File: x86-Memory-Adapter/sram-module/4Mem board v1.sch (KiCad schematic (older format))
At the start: 35 parts, among them K1 CONN_3, P1 CONN_1, P11 CONN_2X2, P2 CONN_1, P3 CONN_1, P4 CONN_1, P8 CONN_20X2, P9 CONN_20X2, U1 SRAM_128KB, U14 XC9536XL-VQ44, U2 SRAM_128KB, U3 SRAM_128KB, U4 SRAM_128KB, U7 LM1086CS_TO252_DPAK

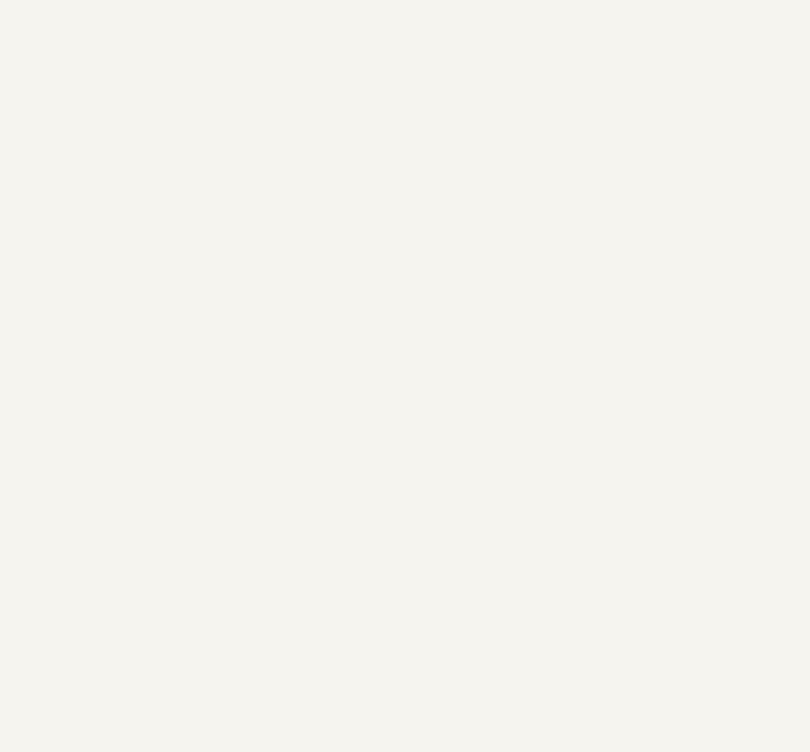
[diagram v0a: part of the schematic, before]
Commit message: x86-Memory-Adapter: SRAM module spare SRAM_512KB symbol (off-sheet)
Source: S100 4GB DRAM BOARD/4Mem board v1 (working folder)
The SRAM_512KB symbol is unannotated, placed outside the sheet and is not in the netlist.
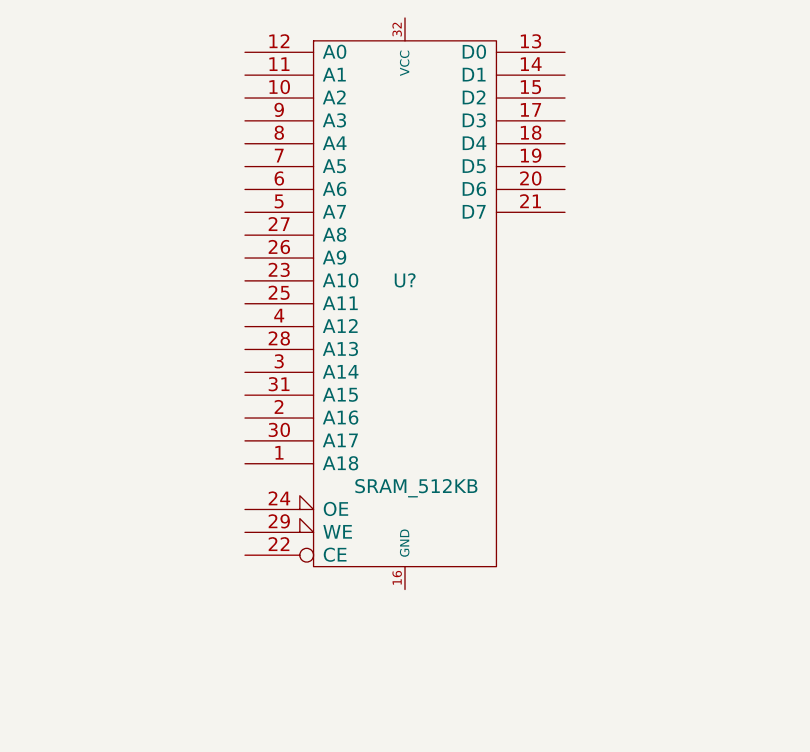
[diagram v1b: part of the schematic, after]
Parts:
- added U?: SRAM_512KB, ~, symbol SRAM_512KB
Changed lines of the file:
@@
 LIBS:numato_kicad_lib
 LIBS:ANTS_MOD1
+LIBS:xc6slx45-2fgg484c
 LIBS:4Mem board v1-cache
 EELAYER 27 0
@@
 Sheet 1 1
 Title "noname.sch"
-Date "29 apr 2015"
+Date "11 jan 2016"
 Rev ""
 Comp ""
@@
 	1    0    0    -1
 $EndComp
+$Comp
+L SRAM_512KB U?
+U 1 1 56937325
+P 12800 -2650
+F 0 "U?" H 12800 -2550 60  0000 C CNN
+F 1 "SRAM_512KB" H 12850 -3450 60  0000 C CNN
+F 2 "~" H 12800 -2650 60  0000 C CNN
+F 3 "~" H 12800 -2650 60  0000 C CNN
+	1    12800 -2650
+	1    0    0    -1
+$EndComp
